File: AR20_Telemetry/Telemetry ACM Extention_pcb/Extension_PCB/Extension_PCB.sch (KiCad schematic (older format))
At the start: 1 part

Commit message: dd
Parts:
- added A1: Arduino_UNO_R3, MCP25625_Breakoutboard:Arduino_UNO_R3_WithMountingHoles_telemetry, symbol MCU_Module:Arduino_UNO_R3
- U1: renamed from U?; footprint (none) -> MCP25625_Breakoutboard:ACM_2020_Footprint
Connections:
- net at U1.28 (5V): now also A1.8 (VIN)
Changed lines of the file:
@@
 EESchema Schematic File Version 4
+LIBS:Extension_PCB-cache
 EELAYER 30 0
 EELAYER END
@@
 $EndDescr
 $Comp
-L ACM_2020_Symbol:ACM_2020 U?
+L ACM_2020_Symbol:ACM_2020 U1
 U 1 1 5E20AD4D
 P 4600 5300
-F 0 "U?" H 4625 7865 50  0000 C CNN
+F 0 "U1" H 4625 7865 50  0000 C CNN
 F 1 "ACM_2020" H 4625 7774 50  0000 C CNN
-F 2 "" H 4600 5300 50  0001 C CNN
+F 2 "MCP25625_Breakoutboard:ACM_2020_Footprint" H 4600 5300 50  0001 C CNN
 F 3 "" H 4600 5300 50  0001 C CNN
 	1    4600 5300
 	1    0    0    -1
 $EndComp
+$Comp
+L MCU_Module:Arduino_UNO_R3 A1
+U 1 1 5E22F864
+P 7850 4000
+F 0 "A1" H 7850 5181 50  0000 C CNN
+F 1 "Arduino_UNO_R3" H 7850 5090 50  0000 C CNN
+F 2 "MCP25625_Breakoutboard:Arduino_UNO_R3_WithMountingHoles_telemetry" H 8000 2950 50  0001 L CNN
+F 3 "https://www.arduino.cc/en/Main/arduinoBoardUno" H 7650 5050 50  0001 C CNN
+	1    7850 4000
+	1    0    0    -1
+$EndComp
+Wire Wire Line
+	7750 3000 5850 3000
+Wire Wire Line
+	5850 3000 5850 4800
+Wire Wire Line
+	5850 4800 5400 4800
 $EndSCHEMATC

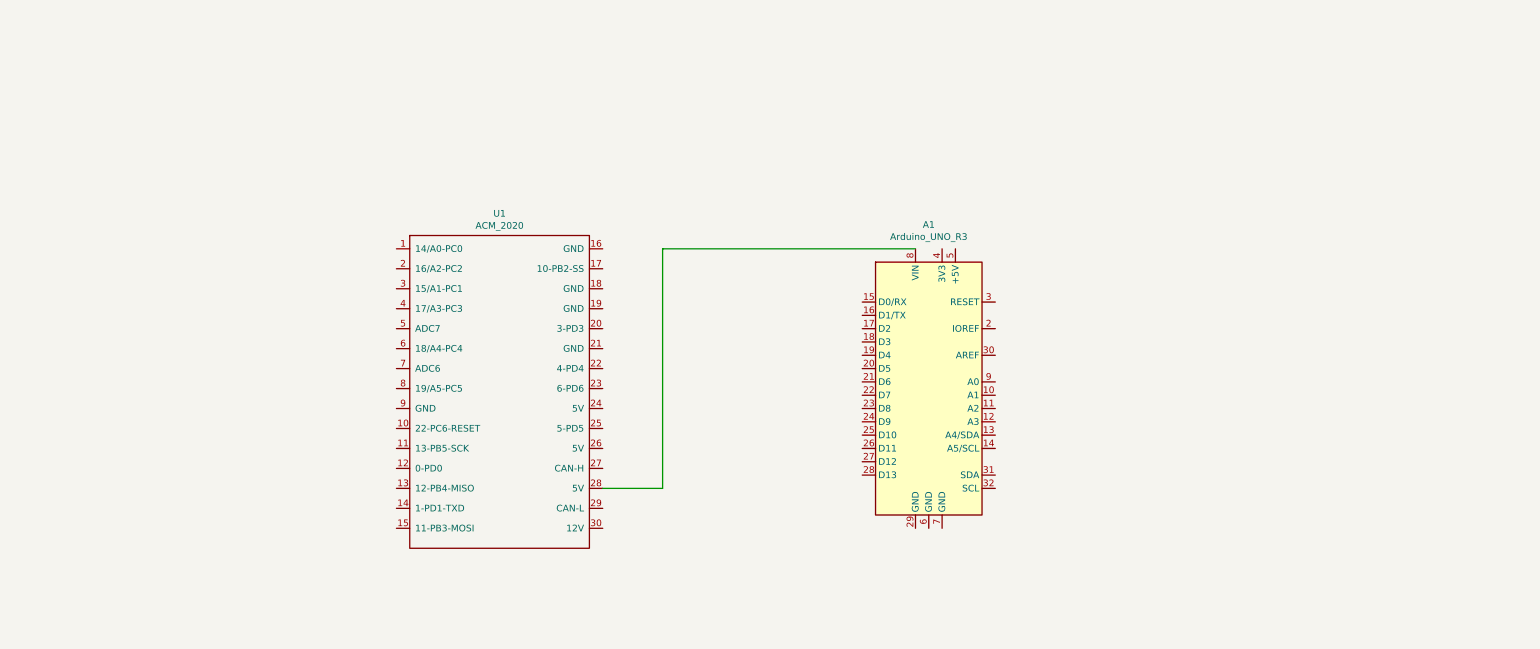
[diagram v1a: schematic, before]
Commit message: Voltage_Regulator added
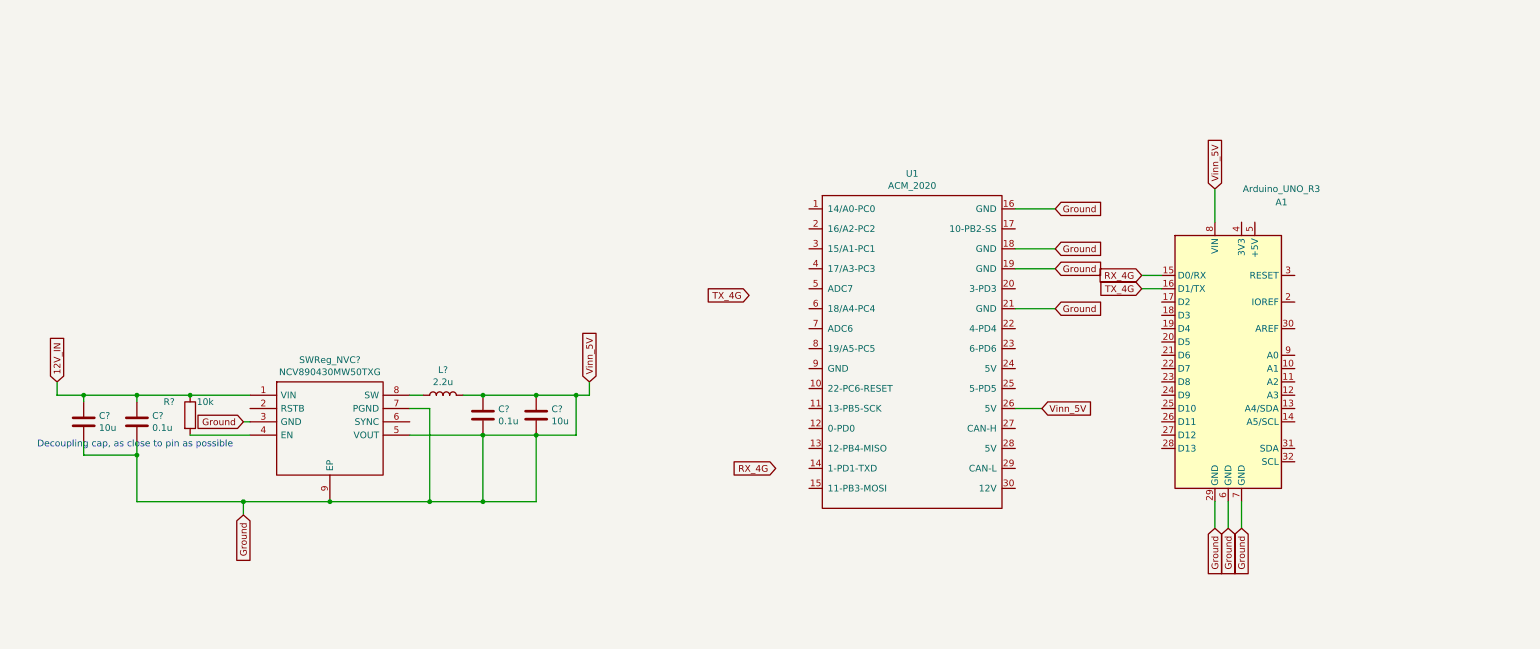
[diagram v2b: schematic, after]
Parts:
- added C? (x2): 0.1u, Capacitor_SMD:C_0603_1608Metric, symbol Device:C
- added C? (x2): 10u, Capacitor_SMD:C_0603_1608Metric, symbol Device:C
- added L?: 2.2u, Inductor_SMD:L_0603_1608Metric, symbol Device:L
- added R?: 10k, Resistor_SMD:R_0603_1608Metric, symbol Device:R
- added SWReg_NVC?: NCV890430MW50TXG, Package_DFN_QFN:DFN-8-1EP_3x3mm_P0.65mm_EP1.7x2.05mm, symbol NCV890430MW50TXG:NCV890430MW50TXG
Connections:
- net Ground: now reaches U1.16 (GND)
- net Ground: now also A1.29 (GND), A1.6 (GND), A1.7 (GND), A1.8 (VIN), U1.18 (GND), U1.19 (GND), U1.21 (GND), U1.26 (5V), C?.1, C?.1, C?.2, C?.2, C?.2, C?.2, L?.2, SWReg_NVC?.3 (GND), SWReg_NVC?.5 (VOUT), SWReg_NVC?.7 (PGND), SWReg_NVC?.9 (EP)
- net at U1.28 (5V): no longer A1.8 (VIN)
- net RX_4G: now reaches A1.15 (D0/RX)
- net TX_4G: now reaches A1.16 (D1/TX)
- new net: R?.2, SWReg_NVC?.4 (EN)
- new net: L?.1, SWReg_NVC?.8 (SW)
- new net 12V_IN: C?.1, C?.1, R?.1, SWReg_NVC?.1 (VIN)
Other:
- note added: "Decoupling cap, as close to pin as possible\n"
- moved on the sheet: A1, U1

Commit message: Edited
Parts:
- removed U1: ACM_2020, MCP25625_Breakoutboard:ACM_2020_Footprint, symbol ACM_2020_Symbol:ACM_2020
- added IC1: MCP25625T-E_ML, QFN65P600X600X100-29N-D, symbol MCP25625T-E_ML:MCP25625T-E_ML
- gave numbers to parts that had none: 7
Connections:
- net Ground: now also IC1.11 (VIO), IC1.22 (GND), IC1.29 (EXP), IC1.3 (VDD)
- net RX_4G: now also IC1.16 (TXD)
- net TX_4G: now also IC1.10 (RXD)
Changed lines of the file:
@@
 $EndDescr
-$Comp
-L ACM_2020_Symbol:ACM_2020 U1
-U 1 1 5E20AD4D
-P 7700 5000
-F 0 "U1" H 7725 7565 50  0000 C CNN
-F 1 "ACM_2020" H 7725 7474 50  0000 C CNN
-F 2 "MCP25625_Breakoutboard:ACM_2020_Footprint" H 7700 5000 50  0001 C CNN
-F 3 "" H 7700 5000 50  0001 C CNN
-	1    7700 5000
-	1    0    0    -1
-$EndComp
 $Comp
 L MCU_Module:Arduino_UNO_R3 A1
@@
 $EndComp
 $Comp
-L NCV890430MW50TXG:NCV890430MW50TXG SWReg_NVC?
+L NCV890430MW50TXG:NCV890430MW50TXG SWReg_NVC1
 U 1 1 5DFC1FB6
 P 2750 4100
-F 0 "SWReg_NVC?" H 3350 4365 50  0000 C CNN
+F 0 "SWReg_NVC1" H 3350 4365 50  0000 C CNN
 F 1 "NCV890430MW50TXG" H 3350 4274 50  0000 C CNN
 F 2 "Package_DFN_QFN:DFN-8-1EP_3x3mm_P0.65mm_EP1.7x2.05mm" H 3800 4200 50  0001 L CNN
@@
 $EndComp
 $Comp
-L Device:C C?
+L Device:C C2
 U 1 1 5DFC1FBC
 P 1900 4300
-F 0 "C?" H 2015 4346 50  0000 L CNN
+F 0 "C2" H 2015 4346 50  0000 L CNN
 F 1 "0.1u" H 2015 4255 50  0000 L CNN
 F 2 "Capacitor_SMD:C_0603_1608Metric" H 1938 4150 50  0001 C CNN
@@
 $EndComp
 $Comp
-L Device:C C?
+L Device:C C1
 U 1 1 5DFC1FC2
 P 1500 4300
-F 0 "C?" H 1615 4346 50  0000 L CNN
+F 0 "C1" H 1615 4346 50  0000 L CNN
 F 1 "10u" H 1615 4255 50  0000 L CNN
 F 2 "Capacitor_SMD:C_0603_1608Metric" H 1538 4150 50  0001 C CNN
@@
 $EndComp
 $Comp
-L Device:C C?
+L Device:C C3
 U 1 1 5DFC1FC8
 P 4500 4250
-F 0 "C?" H 4615 4296 50  0000 L CNN
+F 0 "C3" H 4615 4296 50  0000 L CNN
 F 1 "0.1u" H 4615 4205 50  0000 L CNN
 F 2 "Capacitor_SMD:C_0603_1608Metric" H 4538 4100 50  0001 C CNN
@@
 $EndComp
 $Comp
-L Device:C C?
+L Device:C C4
 U 1 1 5DFC1FCE
 P 4900 4250
-F 0 "C?" H 5015 4296 50  0000 L CNN
+F 0 "C4" H 5015 4296 50  0000 L CNN
 F 1 "10u" H 5015 4205 50  0000 L CNN
 F 2 "Capacitor_SMD:C_0603_1608Metric" H 4938 4100 50  0001 C CNN
@@
 $EndComp
 $Comp
-L Device:L L?
+L Device:L L1
 U 1 1 5DFC1FD4
 P 4200 4100
-F 0 "L?" V 4390 4100 50  0000 C CNN
+F 0 "L1" V 4390 4100 50  0000 C CNN
 F 1 "2.2u" V 4299 4100 50  0000 C CNN
 F 2 "Inductor_SMD:L_0603_1608Metric" H 4200 4100 50  0001 C CNN
@@
 Vinn_5V
 $Comp
-L Device:R R?
+L Device:R R1
 U 1 1 5DFC1FFA
 P 2300 4250
-F 0 "R?" H 2100 4350 50  0000 L CNN
+F 0 "R1" H 2100 4350 50  0000 L CNN
 F 1 "10k" H 2350 4350 50  0000 L CNN
 F 2 "Resistor_SMD:R_0603_1608Metric" V 2230 4250 50  0001 C CNN
@@
 Wire Wire Line
 	4900 4400 5200 4400
-Text GLabel 8700 4200 2    50   Input ~ 0
+Text GLabel 6800 3550 0    50   Input ~ 0
 Vinn_5V
 Text GLabel 10000 2550 1    50   Input ~ 0
@@
 	10000 2800 10000 2550
 Wire Wire Line
-	8700 4200 8500 4200
+	6800 3550 7000 3550
 Text GLabel 10000 5100 3    50   Input ~ 0
 Ground
@@
 Text GLabel 10200 5100 3    50   Input ~ 0
 Ground
-Text GLabel 8800 3450 2    50   Input ~ 0
-Ground
-Text GLabel 8800 3150 2    50   Input ~ 0
-Ground
-Text GLabel 8800 3000 2    50   Input ~ 0
-Ground
-Text GLabel 8800 2700 2    50   Input ~ 0
-Ground
-Wire Wire Line
-	8800 2700 8500 2700
-Wire Wire Line
-	8500 3000 8800 3000
-Wire Wire Line
-	8800 3150 8500 3150
-Wire Wire Line
-	8500 3450 8800 3450
+Text GLabel 7300 2350 1    50   Input ~ 0
+Ground
+Text GLabel 8000 2350 1    50   Input ~ 0
+Ground
+Wire Wire Line
+	8000 2350 8000 2650
+Wire Wire Line
+	7300 2650 7300 2350
 Wire Wire Line
 	10000 5100 10000 4900
@@
 Wire Wire Line
 	9450 3300 9600 3300
-Text GLabel 6700 4650 0    50   Input ~ 0
+Text GLabel 8500 3850 2    50   Input ~ 0
 RX_4G
-Text GLabel 6500 3350 0    50   Input ~ 0
+Text GLabel 7500 4950 3    50   Input ~ 0
 TX_4G
+$Comp
+L MCP25625T-E_ML:MCP25625T-E_ML IC1
+U 1 1 5E4084EF
+P 7000 3350
+F 0 "IC1" H 8344 3046 50  0000 L CNN
+F 1 "MCP25625T-E_ML" H 8344 2955 50  0000 L CNN
+F 2 "QFN65P600X600X100-29N-D" H 8150 3850 50  0001 L CNN
+F 3 "https://www.mouser.com/datasheet/2/268/20005282B-708896.pdf" H 8150 3750 50  0001 L CNN
+F 4 "Microchip Technology MCP25625T-E/ML, CAN Controller 1Mbit/s CAN 2.0B, 28-Pin QFN" H 8150 3650 50  0001 L CNN "Description"
+F 5 "1" H 8150 3550 50  0001 L CNN "Height"
+F 6 "Microchip" H 8150 3450 50  0001 L CNN "Manufacturer_Name"
+F 7 "MCP25625T-E/ML" H 8150 3350 50  0001 L CNN "Manufacturer_Part_Number"
+F 8 "579-MCP25625T-E/ML" H 8150 3250 50  0001 L CNN "Mouser Part Number"
+F 9 "https://www.mouser.com/Search/Refine.aspx?Keyword=579-MCP25625T-E%2FML" H 8150 3150 50  0001 L CNN "Mouser Price/Stock"
+F 10 "1773171P" H 8150 3050 50  0001 L CNN "RS Part Number"
+F 11 "http://uk.rs-online.com/web/p/products/1773171P" H 8150 2950 50  0001 L CNN "RS Price/Stock"
+F 12 "70568355" H 8150 2850 50  0001 L CNN "Allied_Number"
+F 13 "https://www.alliedelec.com/microchiptechnologyinc-mcp25625t-e-ml/70568355/" H 8150 2750 50  0001 L CNN "Allied Price/Stock"
+	1    7000 3350
+	1    0    0    -1
+$EndComp
+Text GLabel 7600 4950 3    50   Input ~ 0
+Vinn_5V
+Wire Wire Line
+	7600 4950 7600 4750
+Wire Wire Line
+	7500 4950 7500 4750
+Wire Wire Line
+	8500 3850 8300 3850
 $EndSCHEMATC

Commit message: Made v0.1
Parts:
- IC1: footprint QFN65P600X600X100-29N-D -> MCP25625_Breakoutboard:QFN65P600X600X100-29N-D
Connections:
- net Ground: no longer A1.8 (VIN), C3.1, C4.1, IC1.11 (VIO), IC1.3 (VDD), L1.2, SWReg_NVC1.5 (VOUT)
- new net Vinn_5V: A1.8 (VIN), C3.1, C4.1, IC1.11 (VIO), IC1.3 (VDD), L1.2, SWReg_NVC1.5 (VOUT)
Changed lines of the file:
@@
 Wire Wire Line
 	3350 4900 4100 4900
-Wire Wire Line
-	3950 4400 4500 4400
-Connection ~ 4500 4400
-Wire Wire Line
-	4500 4400 4900 4400
-Connection ~ 4900 4400
-Wire Wire Line
-	4900 4400 5200 4400
 Text GLabel 6800 3550 0    50   Input ~ 0
 Vinn_5V
@@
 F 0 "IC1" H 8344 3046 50  0000 L CNN
 F 1 "MCP25625T-E_ML" H 8344 2955 50  0000 L CNN
-F 2 "QFN65P600X600X100-29N-D" H 8150 3850 50  0001 L CNN
+F 2 "MCP25625_Breakoutboard:QFN65P600X600X100-29N-D" H 8150 3850 50  0001 L CNN
 F 3 "https://www.mouser.com/datasheet/2/268/20005282B-708896.pdf" H 8150 3750 50  0001 L CNN
 F 4 "Microchip Technology MCP25625T-E/ML, CAN Controller 1Mbit/s CAN 2.0B, 28-Pin QFN" H 8150 3650 50  0001 L CNN "Description"
@@
 Wire Wire Line
 	8500 3850 8300 3850
+Wire Wire Line
+	3950 4400 5200 4400
 $EndSCHEMATC

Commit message: Connector footprint added
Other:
- note added: "MCP25625\n"
- note added: "RX going out of MCP25625, TX going in to MCP25625\nRX is connected to TX intern in ARDUINO(Telemetry module), TX is connected intern to RX in ARDUINO(Telemetry module)"
- note added: "Switching regulator 12V to 5V"
- note added: "Telemetry module (ARDUINO)"
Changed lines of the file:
@@
 Wire Wire Line
 	3950 4400 5200 4400
+Text Notes 3500 5900 0    79   Italic 0
+RX going out of MCP25625, TX going in to MCP25625\nRX is connected to TX intern in ARDUINO(Telemetry module), TX is connected intern to RX in ARDUINO(Telemetry module)
+Wire Notes Line
+	950  3450 950  5450
+Wire Notes Line
+	950  5450 5750 5450
+Wire Notes Line
+	5750 5450 5750 3450
+Wire Notes Line
+	5750 3450 950  3450
+Wire Notes Line
+	6200 5350 8900 5350
+Wire Notes Line
+	8900 5350 8900 1350
+Wire Notes Line
+	8900 1350 6200 1350
+Wire Notes Line
+	6200 1350 6200 5350
+Wire Notes Line
+	8950 1350 8950 5650
+Wire Notes Line
+	8950 5650 11050 5650
+Wire Notes Line
+	11050 5650 11050 1350
+Wire Notes Line
+	11050 1350 8950 1350
+Text Notes 9750 1300 0    50   ~ 0
+MCP25625\n
+Text Notes 6950 1300 0    50   ~ 0
+Telemetry module (ARDUINO)
+Text Notes 2750 3400 0    50   ~ 0
+Switching regulator 12V to 5V
 $EndSCHEMATC

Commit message: Connector added
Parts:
- added J1: MX23A12NF1, MCP25625_Breakoutboard:MX23A12NF1, symbol MCP25625T-E_ML:MX23A12NF1
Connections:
- net 12V_IN: now also J1.6
- net Ground: now also J1.10, J1.11, J1.13, J1.14, J1.8, J1.9
- net Vinn_5V: now also J1.12, J1.3, J1.4, J1.5, J1.7
- net CANL: now reaches IC1.12 (CANL)
- net CANL: now also J1.1
- net CANH: now reaches IC1.13 (CANH)
- net CANH: now also J1.2
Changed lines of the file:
@@
 Decoupling cap, as close to pin as possible\n
 Connection ~ 3350 4900
-Wire Wire Line
-	3350 4900 4100 4900
 Text GLabel 6800 3550 0    50   Input ~ 0
 Vinn_5V
@@
 Wire Notes Line
 	11050 1350 8950 1350
-Text Notes 9750 1300 0    50   ~ 0
+Text Notes 7450 1300 0    50   ~ 0
 MCP25625\n
-Text Notes 6950 1300 0    50   ~ 0
+Text Notes 9200 1300 0    50   ~ 0
 Telemetry module (ARDUINO)
 Text Notes 2750 3400 0    50   ~ 0
 Switching regulator 12V to 5V
+$Comp
+L MCP25625T-E_ML:MX23A12NF1 J1
+U 1 1 5E41E365
+P 2650 1750
+F 0 "J1" H 3100 2015 50  0000 C CNN
+F 1 "MX23A12NF1" H 3100 1924 50  0000 C CNN
+F 2 "MCP25625_Breakoutboard:MX23A12NF1" H 3400 1850 50  0001 L CNN
+F 3 "https://www.jae.com/z-en/pdf_download_exec.cfm?param=SJ100917.pdf" H 3400 1750 50  0001 L CNN
+F 4 "JAE MX23A Series, 2.5mm Pitch 12 Way 2 Row Right Angle PCB Header, Solder Termination, 3A" H 3400 1650 50  0001 L CNN "Description"
+F 5 "16" H 3400 1550 50  0001 L CNN "Height"
+F 6 "JAE Electronics" H 3400 1450 50  0001 L CNN "Manufacturer_Name"
+F 7 "MX23A12NF1" H 3400 1350 50  0001 L CNN "Manufacturer_Part_Number"
+F 8 "656-MX23A12NF1" H 3400 1250 50  0001 L CNN "Mouser Part Number"
+F 9 "https://www.mouser.com/Search/Refine.aspx?Keyword=656-MX23A12NF1" H 3400 1150 50  0001 L CNN "Mouser Price/Stock"
+F 10 "0435780" H 3400 1050 50  0001 L CNN "RS Part Number"
+F 11 "http://uk.rs-online.com/web/p/products/0435780" H 3400 950 50  0001 L CNN "RS Price/Stock"
+	1    2650 1750
+	1    0    0    -1
+$EndComp
+Wire Wire Line
+	2550 1750 2650 1750
+Wire Wire Line
+	2550 1850 2650 1850
+Wire Wire Line
+	2550 1950 2650 1950
+Wire Wire Line
+	2550 2050 2650 2050
+Wire Wire Line
+	2550 2150 2650 2150
+Wire Wire Line
+	2550 2250 2650 2250
+Wire Wire Line
+	2550 2350 2650 2350
+Wire Wire Line
+	3550 2350 3700 2350
+Wire Wire Line
+	3550 2250 3700 2250
+Wire Wire Line
+	3550 2150 3700 2150
+Wire Wire Line
+	3550 2050 3700 2050
+Wire Wire Line
+	3550 1950 3700 1950
+Wire Wire Line
+	3550 1850 3700 1850
+Wire Wire Line
+	3550 1750 3700 1750
+Wire Wire Line
+	3350 4900 4100 4900
+Text GLabel 7800 4950 3    50   Input ~ 0
+CANH
+Wire Wire Line
+	7700 4750 7700 4950
+Wire Wire Line
+	7800 4750 7800 4950
+Text GLabel 2550 1850 0    50   Input ~ 0
+CANH
+Text GLabel 7700 4950 3    50   Input ~ 0
+CANL
+Text GLabel 2550 1750 0    50   Input ~ 0
+CANL
+Text GLabel 2550 1950 0    50   Input ~ 0
+Vinn_5V
+Text GLabel 2550 2350 0    50   Input ~ 0
+Vinn_5V
+Text GLabel 2550 2150 0    50   Input ~ 0
+Vinn_5V
+Text GLabel 2550 2050 0    50   Input ~ 0
+Vinn_5V
+Text GLabel 3700 2150 2    50   Input ~ 0
+Vinn_5V
+Text GLabel 3700 1750 2    50   Input ~ 0
+Ground
+Text GLabel 3700 2050 2    50   Input ~ 0
+Ground
+Text GLabel 3700 1950 2    50   Input ~ 0
+Ground
+Text GLabel 3700 1850 2    50   Input ~ 0
+Ground
+Text GLabel 2550 2250 0    50   Input ~ 0
+12V_IN
+Text GLabel 3700 2250 2    50   Input ~ 0
+Ground
+Text GLabel 3700 2350 2    50   Input ~ 0
+Ground
 $EndSCHEMATC
